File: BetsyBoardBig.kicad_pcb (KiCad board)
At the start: 4 copper layers, 48 x 48 mm, 78 parts, among them J1 USB_C_Receptacle_USB2.0, J2 CLOCKS, J3 SPI, J4 I2C, J5 USART3, J6 ANALOG, J7 USART1, J8 Micro_SD_Card, P1 BATT, P2 BATT, P3 CORTEX-JTAG, SW1 JUMPER, SW2 TE-FSM4J, SW3 SW_PUSH_NO_ALT, U1 TLV75733PDBVR‎, U2 USBLC6-2SC6, U3 MCP73871, U4 74LVC1G08, U5 74LVC3G14, U6 STM32L486Rx-LQFP64, U7 74LVC1G3157, U8 IS25LP06D-xB, X1 XTAL, Y1 Crystal

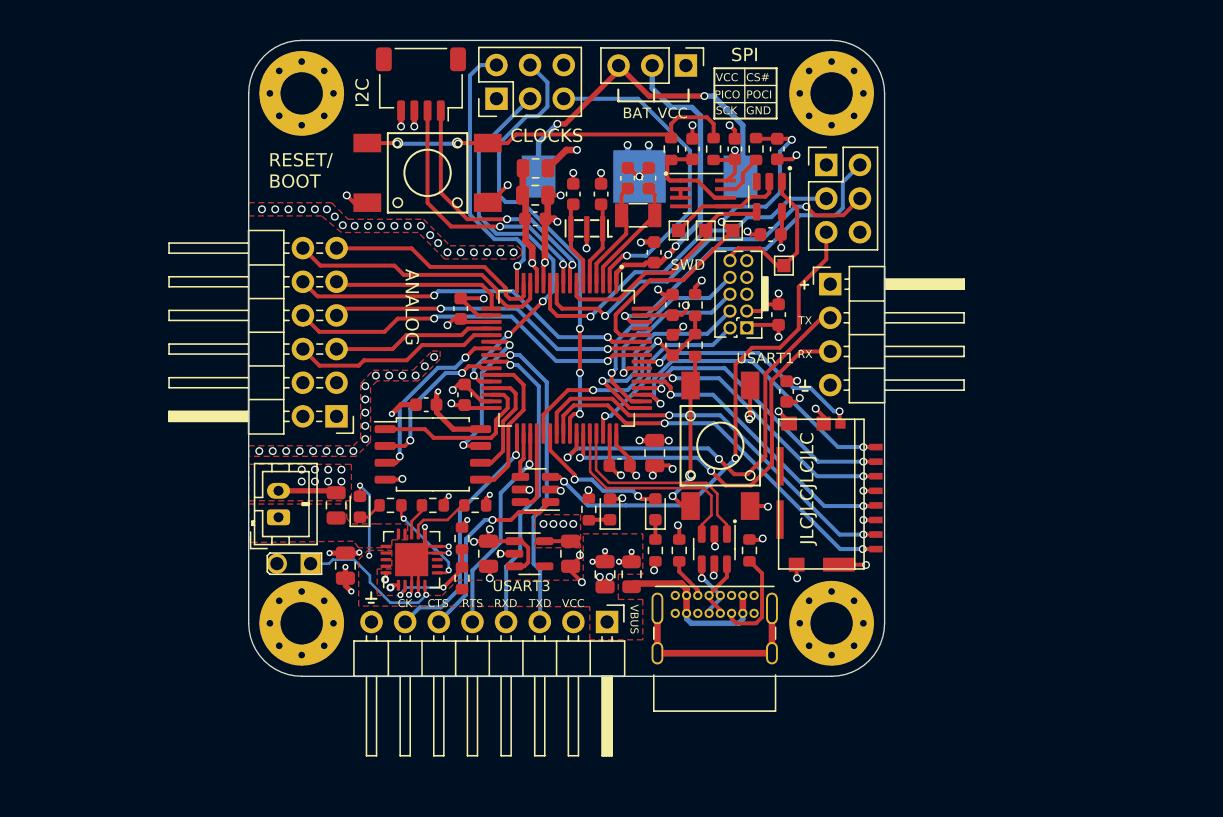
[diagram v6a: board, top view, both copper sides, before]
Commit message: Reworking reset pin on JTAG/SWD header and adding AND-gate.
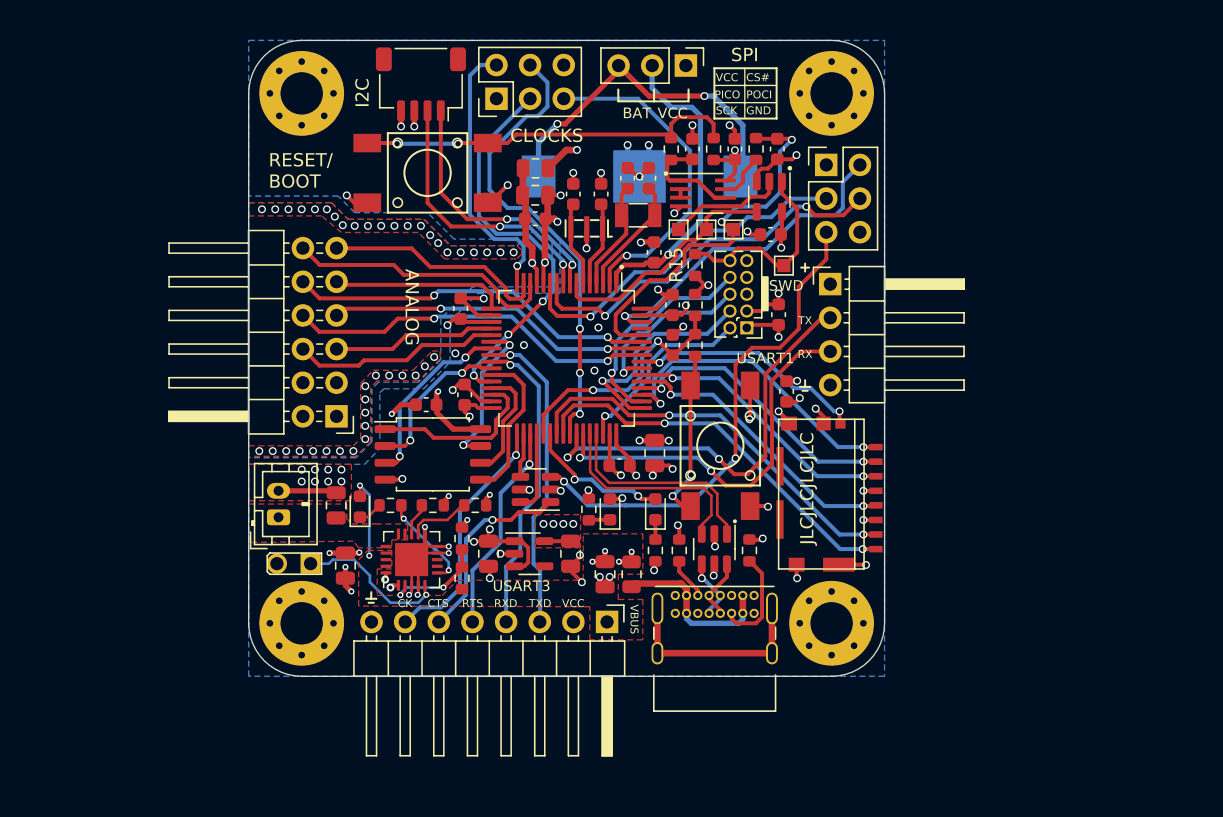
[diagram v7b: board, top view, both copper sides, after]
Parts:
- added R15: 10K, Resistor_SMD:R_0603_1608Metric, F.Cu at (129.7, 68.0)
- moved TP1 0.09 mm to (130.6, 65.3)
- moved TP4 0.09 mm to (132.6, 65.3)
- moved TP2 0.07 mm to (128.4, 65.3)
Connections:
- U6 pad 61: /PB8 -> unconnected-(U6-PB8/I2C1_SCL/SDD4-Pad61)
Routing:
- net GND: track 101.9 -> 105.2 mm, vias 64 -> 69
- net /~{JTRST}: track 12.4 -> 15.3 mm
- net /BOOT0: track 28.3 -> 29.3 mm
- net /VCOIN: track 23.8 -> 23.0 mm, vias 2 -> 1
- net /OCLK_M: track 34.2 -> 35.0 mm
- added copper zone on B.Cu, net GND
- added copper zone on B.Cu, net VSSA
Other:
- board text added: "PA3/PB7"
- board text removed: "PA2/PB7"
